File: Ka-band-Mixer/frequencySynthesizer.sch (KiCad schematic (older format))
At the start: 30 parts, among them J4 Conn_01x05_Male, U1 ADF4150HV, X1 IQXT-220-1

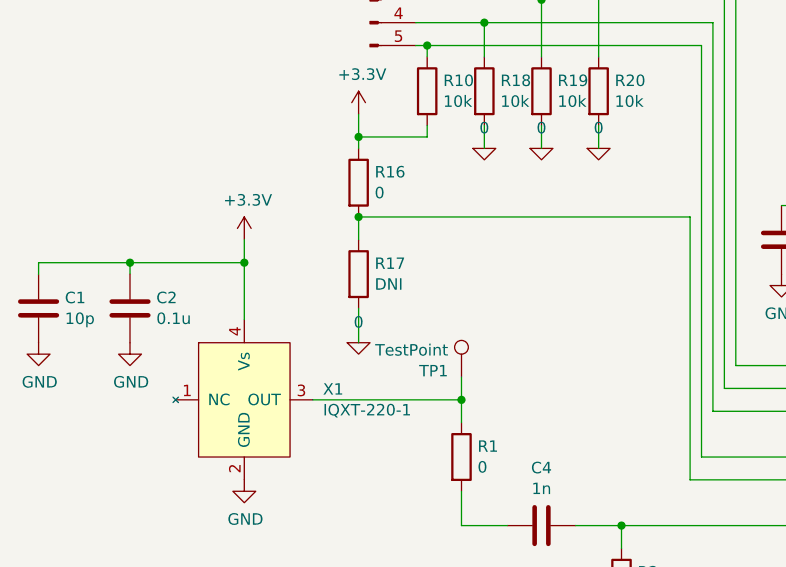
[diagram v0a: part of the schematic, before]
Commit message: Remove PullDown PDBRF
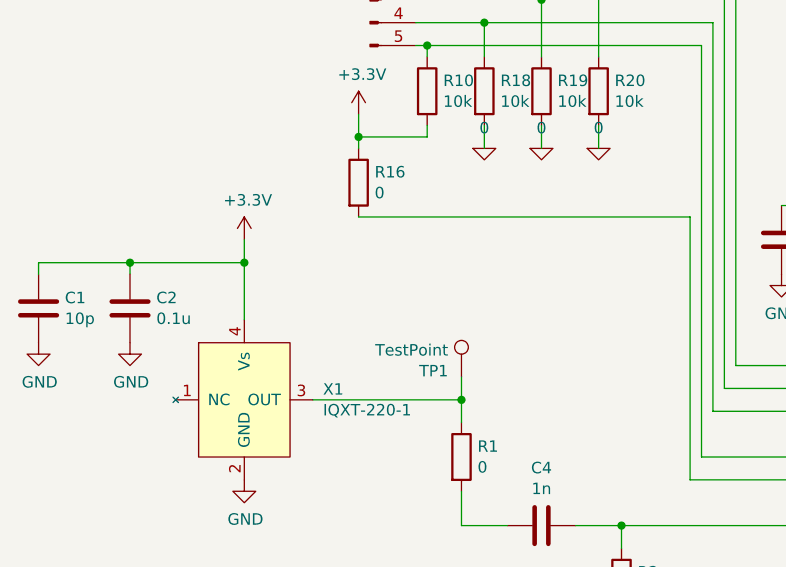
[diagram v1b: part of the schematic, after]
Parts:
- removed R17: DNI, Resistor_SMD:R_0603_1608Metric_Pad0.98x0.95mm_HandSolder, symbol Device:R
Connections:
- wire segments 102 -> 100
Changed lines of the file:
@@
 Wire Wire Line
 	3500 1500 3750 1500
-$Comp
-L Device:R R17
-U 1 1 5FD3B0E5
-P 2700 3000
-F 0 "R17" H 2770 3046 50  0000 L CNN
-F 1 "DNI" H 2770 2955 50  0000 L CNN
-F 2 "Resistor_SMD:R_0603_1608Metric_Pad0.98x0.95mm_HandSolder" V 2630 3000 50  0001 C CNN
-F 3 "~" H 2700 3000 50  0001 C CNN
-F 4 "D/CRCW0402 kit in dipartimento" H 2700 3000 50  0001 C CNN "Supplier Stock Code"
-	1    2700 3000
-	1    0    0    -1
-$EndComp
-Wire Wire Line
-	2700 3150 2700 3300
-Wire Wire Line
-	2700 2750 2700 2850
-$Comp
-L pspice:0 #GND0123
-U 1 1 5FD49CF4
-P 2700 3300
-F 0 "#GND0123" H 2700 3200 50  0001 C CNN
-F 1 "0" H 2700 3389 50  0000 C CNN
-F 2 "" H 2700 3300 50  0001 C CNN
-F 3 "~" H 2700 3300 50  0001 C CNN
-	1    2700 3300
-	1    0    0    -1
-$EndComp
 Connection ~ 5250 2700
 Wire Wire Line
@@
 	1    0    0    -1
 $EndComp
-Connection ~ 2700 2750
 Wire Wire Line
 	3000 2050 3000 2000

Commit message: some_update
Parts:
- removed R16: 0, Resistor_SMD:R_0402_1005Metric_Pad0.72x0.64mm_HandSolder, symbol Device:R
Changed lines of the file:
@@
-$EndComp
-$Comp
-L Device:R R16
-U 1 1 5FD46A04
-P 2700 2600
-F 0 "R16" H 2770 2646 50  0000 L CNN
-F 1 "0" H 2770 2555 50  0000 L CNN
-F 2 "Resistor_SMD:R_0402_1005Metric_Pad0.72x0.64mm_HandSolder" V 2630 2600 50  0001 C CNN
-F 3 "~" H 2700 2600 50  0001 C CNN
-F 4 "D/CRCW0402 kit in dipartimento" H 2700 2600 50  0001 C CNN "Supplier Stock Code"
-	1    2700 2600
-	1    0    0    -1
 $EndComp
 $Comp
@@
 	3000 2400 2700 2400
 Connection ~ 2700 2400
-Wire Wire Line
-	2700 2400 2700 2450
 $Comp
 L Device:R R18
@@
 	3150 3450 3150 3550
 Connection ~ 3150 3550
+Wire Wire Line
+	2700 2400 2700 2750
 $EndSCHEMATC

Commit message: Update BOM
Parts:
- C1, C11, C12, C8: Manufacturer/Part Number GRM1555C2A100GA01D -> 04025A100JAT2A; Supplier Stock Code Mouser 81-GRM1555C2A100GA1D -> 581-04025A100J
- C10: Manufacturer/Part Number C0402C104J8RACAUTO -> 963-GMK105CC6105MV-F; Supplier Stock Code Mouser 80-C0402C104J8RAUTO -> GMK105CC6105MV-F
- C13: Manufacturer/Part Number GCM155R71H331KA37J -> GRM022R71C331KE14L; Supplier Stock Code Mouser 881-GCM155R71H331KA7J -> 81-GRM022R71C331KE4L
- C14: Supplier Stock Code Mouser 81-GCM155R71H562JA5D -> 81-GCM155R71H562JA5D
- C15: Manufacturer/Part Number GCM1555C1H121JA16D -> 04023A121JAT2A; Supplier Stock Code Mouser 81-GCM1555C1H121JA6D -> 581-04023A121JAT2A
- C2: Manufacturer/Part Number C0402C104J8RACAUTO -> 581-0402YD104MAT2A; Supplier Stock Code Mouser 80-C0402C104J8RAUTO -> 0402YD104MAT2A
- C4: Manufacturer/Part Number GRM1555C1H102FA01D -> 04025C102JAT2A; Supplier Stock Code Mouser 81-GRM1555C1H102FA1D -> 581-04025C102J
- C6: Supplier Stock Code Mouser 81-GCM1555C1H101JA6D -> 81-GCM1555C1H101JA6D
- C7, C9: Manufacturer/Part Number C0402C104J8RACAUTO -> 0402YD104MAT2A; Supplier Stock Code Mouser 80-C0402C104J8RAUTO -> 581-0402YD104MAT2A
- D1: Supplier Stock Code Mouser 630-HSMG-C170 -> 630-HSMG-C170
- X1: Manufacturer/Part Number (none) -> HMC292ALC3B; Supplier Stock Code (none) -> 584-HMC292ALC3B
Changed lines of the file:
@@
 F 2 "Capacitor_SMD:C_0402_1005Metric_Pad0.74x0.62mm_HandSolder" H 4988 2700 50  0001 C CNN
 F 3 "~" H 4950 2850 50  0001 C CNN
-F 4 "GRM1555C2A100GA01D" H 4950 2850 50  0001 C CNN "Manufacturer/Part Number"
-F 5 "Mouser 81-GRM1555C2A100GA1D" H 4950 2850 50  0001 C CNN "Supplier Stock Code"
+F 4 "04025A100JAT2A" H 4950 2850 50  0001 C CNN "Manufacturer/Part Number"
+F 5 "581-04025A100J" H 4950 2850 50  0001 C CNN "Supplier Stock Code"
 	1    4950 2850
 	-1   0    0    1
@@
 F 2 "Capacitor_SMD:C_0402_1005Metric_Pad0.74x0.62mm_HandSolder" H 4588 2700 50  0001 C CNN
 F 3 "~" H 4550 2850 50  0001 C CNN
-F 4 "Mouser 80-C0402C104J8RAUTO" H 4550 2850 50  0001 C CNN "Supplier Stock Code"
-F 5 "C0402C104J8RACAUTO" H 4550 2850 50  0001 C CNN "Manufacturer/Part Number"
+F 4 "581-0402YD104MAT2A" H 4550 2850 50  0001 C CNN "Supplier Stock Code"
+F 5 "0402YD104MAT2A" H 4550 2850 50  0001 C CNN "Manufacturer/Part Number"
 	1    4550 2850
 	-1   0    0    1
@@
 F 2 "Capacitor_SMD:C_0402_1005Metric_Pad0.74x0.62mm_HandSolder" H 5788 2700 50  0001 C CNN
 F 3 "~" H 5750 2850 50  0001 C CNN
-F 4 "Mouser 80-C0402C104J8RAUTO" H 5750 2850 50  0001 C CNN "Supplier Stock Code"
-F 5 "C0402C104J8RACAUTO" H 5750 2850 50  0001 C CNN "Manufacturer/Part Number"
+F 4 "581-0402YD104MAT2A" H 5750 2850 50  0001 C CNN "Supplier Stock Code"
+F 5 "0402YD104MAT2A" H 5750 2850 50  0001 C CNN "Manufacturer/Part Number"
 	1    5750 2850
 	-1   0    0    1
@@
 F 2 "Capacitor_SMD:C_0402_1005Metric_Pad0.74x0.62mm_HandSolder" H 6188 2700 50  0001 C CNN
 F 3 "~" H 6150 2850 50  0001 C CNN
-F 4 "GRM1555C2A100GA01D" H 6150 2850 50  0001 C CNN "Manufacturer/Part Number"
-F 5 "Mouser 81-GRM1555C2A100GA1D" H 6150 2850 50  0001 C CNN "Supplier Stock Code"
+F 4 "04025A100JAT2A" H 6150 2850 50  0001 C CNN "Manufacturer/Part Number"
+F 5 "581-04025A100J" H 6150 2850 50  0001 C CNN "Supplier Stock Code"
 	1    6150 2850
 	-1   0    0    1
@@
 F 2 "Oscillator:Oscillator_SMD_Abracon_ASE-4Pin_3.2x2.5mm_HandSoldering" H 2200 3550 50  0001 C CNN
 F 3 "https://www.mouser.it/datasheet/2/741/LFTCXO075792Cutt-1115708.pdf" H 2200 3550 50  0001 C CNN
+F 4 "HMC292ALC3B" H 2200 3550 50  0001 C CNN "Manufacturer/Part Number"
+F 5 "584-HMC292ALC3B" H 2200 3550 50  0001 C CNN "Supplier Stock Code"
 	1    2200 3550
 	1    0    0    -1
@@
 F 2 "Capacitor_SMD:C_0402_1005Metric_Pad0.74x0.62mm_HandSolder" H 1738 3000 50  0001 C CNN
 F 3 "~" H 1700 3150 50  0001 C CNN
-F 4 "Mouser 80-C0402C104J8RAUTO" H 1700 3150 50  0001 C CNN "Supplier Stock Code"
-F 5 "C0402C104J8RACAUTO" H 1700 3150 50  0001 C CNN "Manufacturer/Part Number"
+F 4 "0402YD104MAT2A" H 1700 3150 50  0001 C CNN "Supplier Stock Code"
+F 5 "581-0402YD104MAT2A" H 1700 3150 50  0001 C CNN "Manufacturer/Part Number"
 	1    1700 3150
 	-1   0    0    1
@@
 F 2 "Capacitor_SMD:C_0402_1005Metric_Pad0.74x0.62mm_HandSolder" H 1338 3000 50  0001 C CNN
 F 3 "~" H 1300 3150 50  0001 C CNN
-F 4 "GRM1555C2A100GA01D" H 1300 3150 50  0001 C CNN "Manufacturer/Part Number"
-F 5 "Mouser 81-GRM1555C2A100GA1D" H 1300 3150 50  0001 C CNN "Supplier Stock Code"
+F 4 "04025A100JAT2A" H 1300 3150 50  0001 C CNN "Manufacturer/Part Number"
+F 5 "581-04025A100J" H 1300 3150 50  0001 C CNN "Supplier Stock Code"
 	1    1300 3150
 	-1   0    0    1
@@
 F 2 "Capacitor_SMD:C_0402_1005Metric_Pad0.74x0.62mm_HandSolder" H 3538 3950 50  0001 C CNN
 F 3 "~" H 3500 4100 50  0001 C CNN
-F 4 "GRM1555C1H102FA01D" H 3500 4100 50  0001 C CNN "Manufacturer/Part Number"
-F 5 "Mouser 81-GRM1555C1H102FA1D" H 3500 4100 50  0001 C CNN "Supplier Stock Code"
+F 4 "04025C102JAT2A" H 3500 4100 50  0001 C CNN "Manufacturer/Part Number"
+F 5 "581-04025C102J" H 3500 4100 50  0001 C CNN "Supplier Stock Code"
 	1    3500 4100
 	0    1    1    0
@@
 F 2 "Capacitor_SMD:C_0402_1005Metric_Pad0.74x0.62mm_HandSolder" H 6638 3700 50  0001 C CNN
 F 3 "~" H 6600 3850 50  0001 C CNN
-F 4 "GCM155R71H331KA37J" H 6600 3850 50  0001 C CNN "Manufacturer/Part Number"
-F 5 "Mouser 881-GCM155R71H331KA7J" H 6600 3850 50  0001 C CNN "Supplier Stock Code"
+F 4 "GRM022R71C331KE14L" H 6600 3850 50  0001 C CNN "Manufacturer/Part Number"
+F 5 "81-GRM022R71C331KE4L" H 6600 3850 50  0001 C CNN "Supplier Stock Code"
 	1    6600 3850
 	-1   0    0    1
@@
 F 3 "~" H 7050 4050 50  0001 C CNN
 F 4 "GCM155R71H562JA55D" H 7050 4050 50  0001 C CNN "Manufacturer/Part Number"
-F 5 "Mouser 81-GCM155R71H562JA5D" H 7050 4050 50  0001 C CNN "Supplier Stock Code"
+F 5 "81-GCM155R71H562JA5D" H 7050 4050 50  0001 C CNN "Supplier Stock Code"
 	1    7050 4050
 	-1   0    0    1
@@
 F 2 "Capacitor_SMD:C_0402_1005Metric_Pad0.74x0.62mm_HandSolder" H 7788 3600 50  0001 C CNN
 F 3 "~" H 7750 3750 50  0001 C CNN
-F 4 "GCM1555C1H121JA16D" H 7750 3750 50  0001 C CNN "Manufacturer/Part Number"
-F 5 "Mouser 81-GCM1555C1H121JA6D" H 7750 3750 50  0001 C CNN "Supplier Stock Code"
+F 4 "04023A121JAT2A" H 7750 3750 50  0001 C CNN "Manufacturer/Part Number"
+F 5 "581-04023A121JAT2A" H 7750 3750 50  0001 C CNN "Supplier Stock Code"
 	1    7750 3750
 	-1   0    0    1
@@
 F 3 "https://www.mouser.it/datasheet/2/678/av02-0551en-ds-hsmx-cxxx-05mar2012-1827675.pdf" H 6900 5000 50  0001 C CNN
 F 4 "HSMG-C170" H 6900 5000 50  0001 C CNN "Manufacturer/Part Number"
-F 5 "Mouser 630-HSMG-C170" H 6900 5000 50  0001 C CNN "Supplier Stock Code"
+F 5 "630-HSMG-C170" H 6900 5000 50  0001 C CNN "Supplier Stock Code"
 	1    6900 5000
 	0    -1   -1   0
@@
 F 3 "~" H 4300 5300 50  0001 C CNN
 F 4 "GCM1555C1H101JA16D" H 4300 5300 50  0001 C CNN "Manufacturer/Part Number"
-F 5 "Mouser 81-GCM1555C1H101JA6D" H 4300 5300 50  0001 C CNN "Supplier Stock Code"
+F 5 "81-GCM1555C1H101JA6D" H 4300 5300 50  0001 C CNN "Supplier Stock Code"
 	1    4300 5300
 	-1   0    0    1
@@
 F 2 "Capacitor_SMD:C_0402_1005Metric_Pad0.74x0.62mm_HandSolder" H 5888 2050 50  0001 C CNN
 F 3 "~" H 5850 2200 50  0001 C CNN
-F 4 "Mouser 80-C0402C104J8RAUTO" H 5850 2200 50  0001 C CNN "Supplier Stock Code"
-F 5 "C0402C104J8RACAUTO" H 5850 2200 50  0001 C CNN "Manufacturer/Part Number"
+F 4 "GMK105CC6105MV-F" H 5850 2200 50  0001 C CNN "Supplier Stock Code"
+F 5 "963-GMK105CC6105MV-F" H 5850 2200 50  0001 C CNN "Manufacturer/Part Number"
 	1    5850 2200
 	-1   0    0    1
@@
 F 2 "Capacitor_SMD:C_0402_1005Metric_Pad0.74x0.62mm_HandSolder" H 6288 2050 50  0001 C CNN
 F 3 "~" H 6250 2200 50  0001 C CNN
-F 4 "GRM1555C2A100GA01D" H 6250 2200 50  0001 C CNN "Manufacturer/Part Number"
-F 5 "Mouser 81-GRM1555C2A100GA1D" H 6250 2200 50  0001 C CNN "Supplier Stock Code"
+F 4 "04025A100JAT2A" H 6250 2200 50  0001 C CNN "Manufacturer/Part Number"
+F 5 "581-04025A100J" H 6250 2200 50  0001 C CNN "Supplier Stock Code"
 	1    6250 2200
 	-1   0    0    1
